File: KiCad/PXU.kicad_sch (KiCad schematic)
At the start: 0 parts

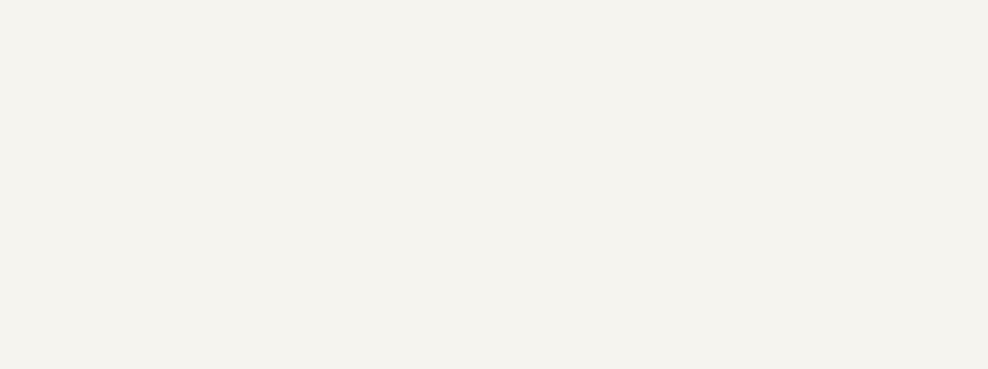
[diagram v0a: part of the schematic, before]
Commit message: License upload
Missed including license in initial upload
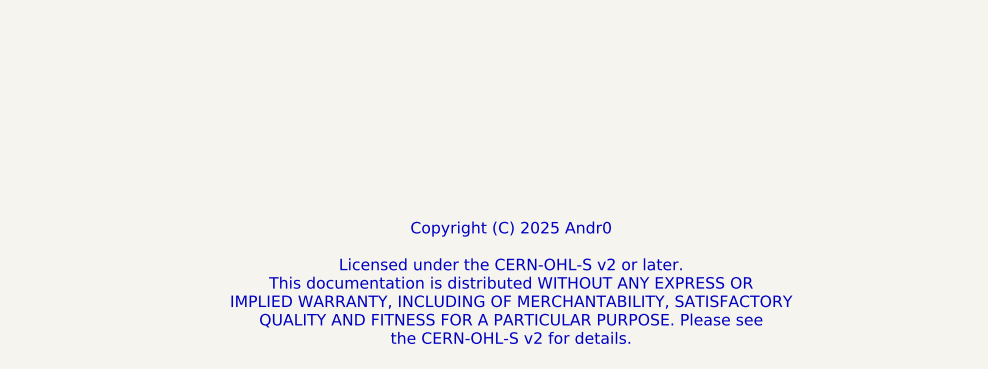
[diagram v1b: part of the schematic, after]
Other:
- note added: "Copyright (C) 2025 Andr0 Licensed under the CERN-OHL-S v2 or later. This documentation is distributed WITHOUT ANY EXPRESS OR IMPLIED WARRANTY, INCLUDING OF MERCHANTABILITY, SATISFACTORY QUALITY AND FITNESS FOR A PARTICULAR PURPOSE. Please see the CERN-OHL-S v2 for details."
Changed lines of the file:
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@@
+		)
+	)
+	(text "Copyright (C) 2025 Andr0\n\nLicensed under the CERN-OHL-S v2 or later.\nThis documentation is distributed WITHOUT ANY EXPRESS OR\nIMPLIED WARRANTY, INCLUDING OF MERCHANTABILITY, SATISFACTORY\nQUALITY AND FITNESS FOR A PARTICULAR PURPOSE. Please see\nthe CERN-OHL-S v2 for details."
+		(exclude_from_sim no)
+		(at 208.788 180.086 0)
+		(effects
+			(font
+				(size 1.27 1.27)
+			)
 		)
 	)
